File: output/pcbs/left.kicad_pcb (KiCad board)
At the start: 2 copper layers, 123.1 x 93.2 mm, 27 parts

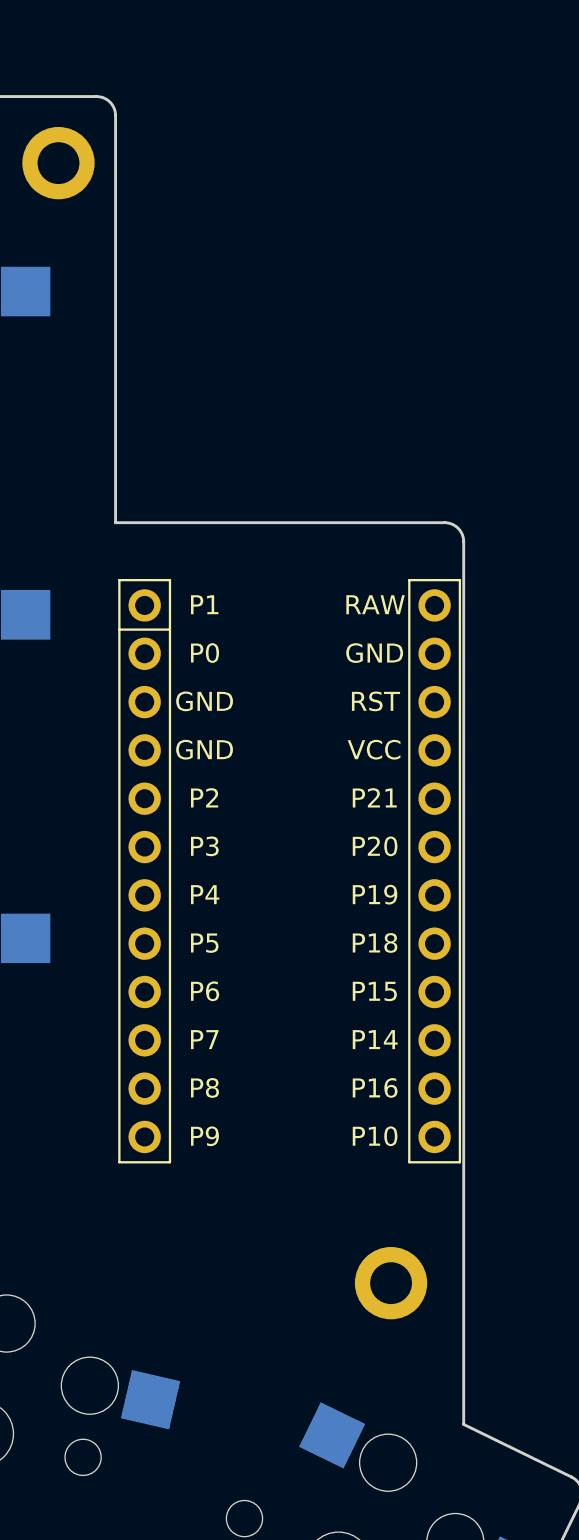
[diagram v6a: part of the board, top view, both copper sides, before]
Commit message: shift the MCU way up
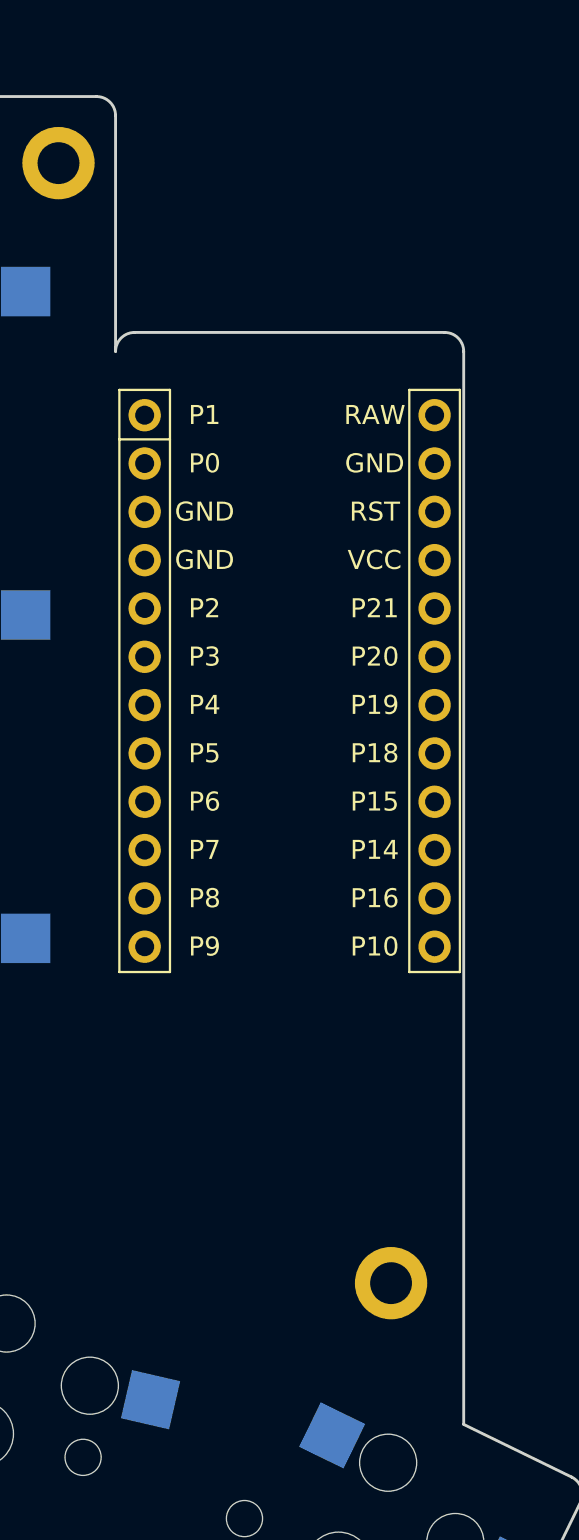
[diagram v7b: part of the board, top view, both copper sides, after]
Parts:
- moved MCU1 10.0 mm to (93.3, -31.4)
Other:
- outline, holes or cut-outs redrawn
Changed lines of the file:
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@@
   (footprint "ceoloide:mcu_nice_nano"
     (layer "F.Cu")
-    (at 93.29836660000001 -21.3657089 0)
+    (at 93.29836660000001 -31.3657089 0)
     (property "Reference" "MCU1"
       (at 0 -15 0)
@@
 (gr_line (start 108.1213601 11.751844899999998) (end 102.44836660000001 8.984941108545392) (layer Edge.Cuts) (stroke (width 0.15) (type default)))
 (gr_line (start 24.54726792343898 -60.815708799999996) (end 25.148366699999997 -60.84721104908856) (layer Edge.Cuts) (stroke (width 0.15) (type default)))
-(gr_line (start 84.1483667 -38.4157089) (end 101.44836660000001 -38.4157089) (layer Edge.Cuts) (stroke (width 0.15) (type default)))
-(gr_line (start 102.44836660000001 8.984941108545392) (end 102.44836660000001 -37.4157089) (layer Edge.Cuts) (stroke (width 0.15) (type default)))
-(gr_arc (start 102.44836660000001 -37.4157089) (mid 102.15547340000002 -38.1228157) (end 101.44836660000001 -38.4157089) (layer Edge.Cuts) (stroke (width 0.15) (type default)))
+(gr_line (start 102.44836660000001 8.984941108545392) (end 102.44836660000001 -47.4157089) (layer Edge.Cuts) (stroke (width 0.15) (type default)))
+(gr_line (start 85.1483666 -48.4157089) (end 101.44836660000001 -48.4157089) (layer Edge.Cuts) (stroke (width 0.15) (type default)))
+(gr_arc (start 85.1483666 -48.4157089) (mid 84.4414179 -48.1229738) (end 84.1483667 -47.4161561) (layer Edge.Cuts) (stroke (width 0.15) (type default)))
+(gr_arc (start 102.44836660000001 -47.4157089) (mid 102.15547340000002 -48.1228157) (end 101.44836660000001 -48.4157089) (layer Edge.Cuts) (stroke (width 0.15) (type default)))
 (gr_line (start -7.851633400000004 16.6842912) (end -8.3250278 16.460374) (layer Edge.Cuts) (stroke (width 0.15) (type default)))
 (gr_line (start -9.851633300000003 -42.7041617200161) (end -9.851633300000003 -59.815708799999996) (layer Edge.Cuts) (stroke (width 0.15) (type default)))
 (gr_line (start -8.851633300000003 -60.815708799999996) (end 24.54726792343898 -60.815708799999996) (layer Edge.Cuts) (stroke (width 0.15) (type default)))
 (gr_line (start 45.148366599999996 -60.815708799999996) (end 83.1483667 -60.815708799999996) (layer Edge.Cuts) (stroke (width 0.15) (type default)))
-(gr_line (start 84.1483667 -59.815708799999996) (end 84.1483667 -38.4157089) (layer Edge.Cuts) (stroke (width 0.15) (type default)))
+(gr_line (start 84.1483667 -59.815708799999996) (end 84.1483667 -47.4161561) (layer Edge.Cuts) (stroke (width 0.15) (type default)))
 (gr_arc (start -8.851633300000003 -60.815708799999996) (mid -9.558740100000003 -60.522815599999994) (end -9.851633300000003 -59.815708799999996) (layer Edge.Cuts) (stroke (width 0.15) (type default)))
 (gr_arc (start 84.1483667 -59.815708799999996) (mid 83.8554735 -60.522815599999994) (end 83.1483667 -60.815708799999996) (layer Edge.Cuts) (stroke (width 0.15) (type default)))

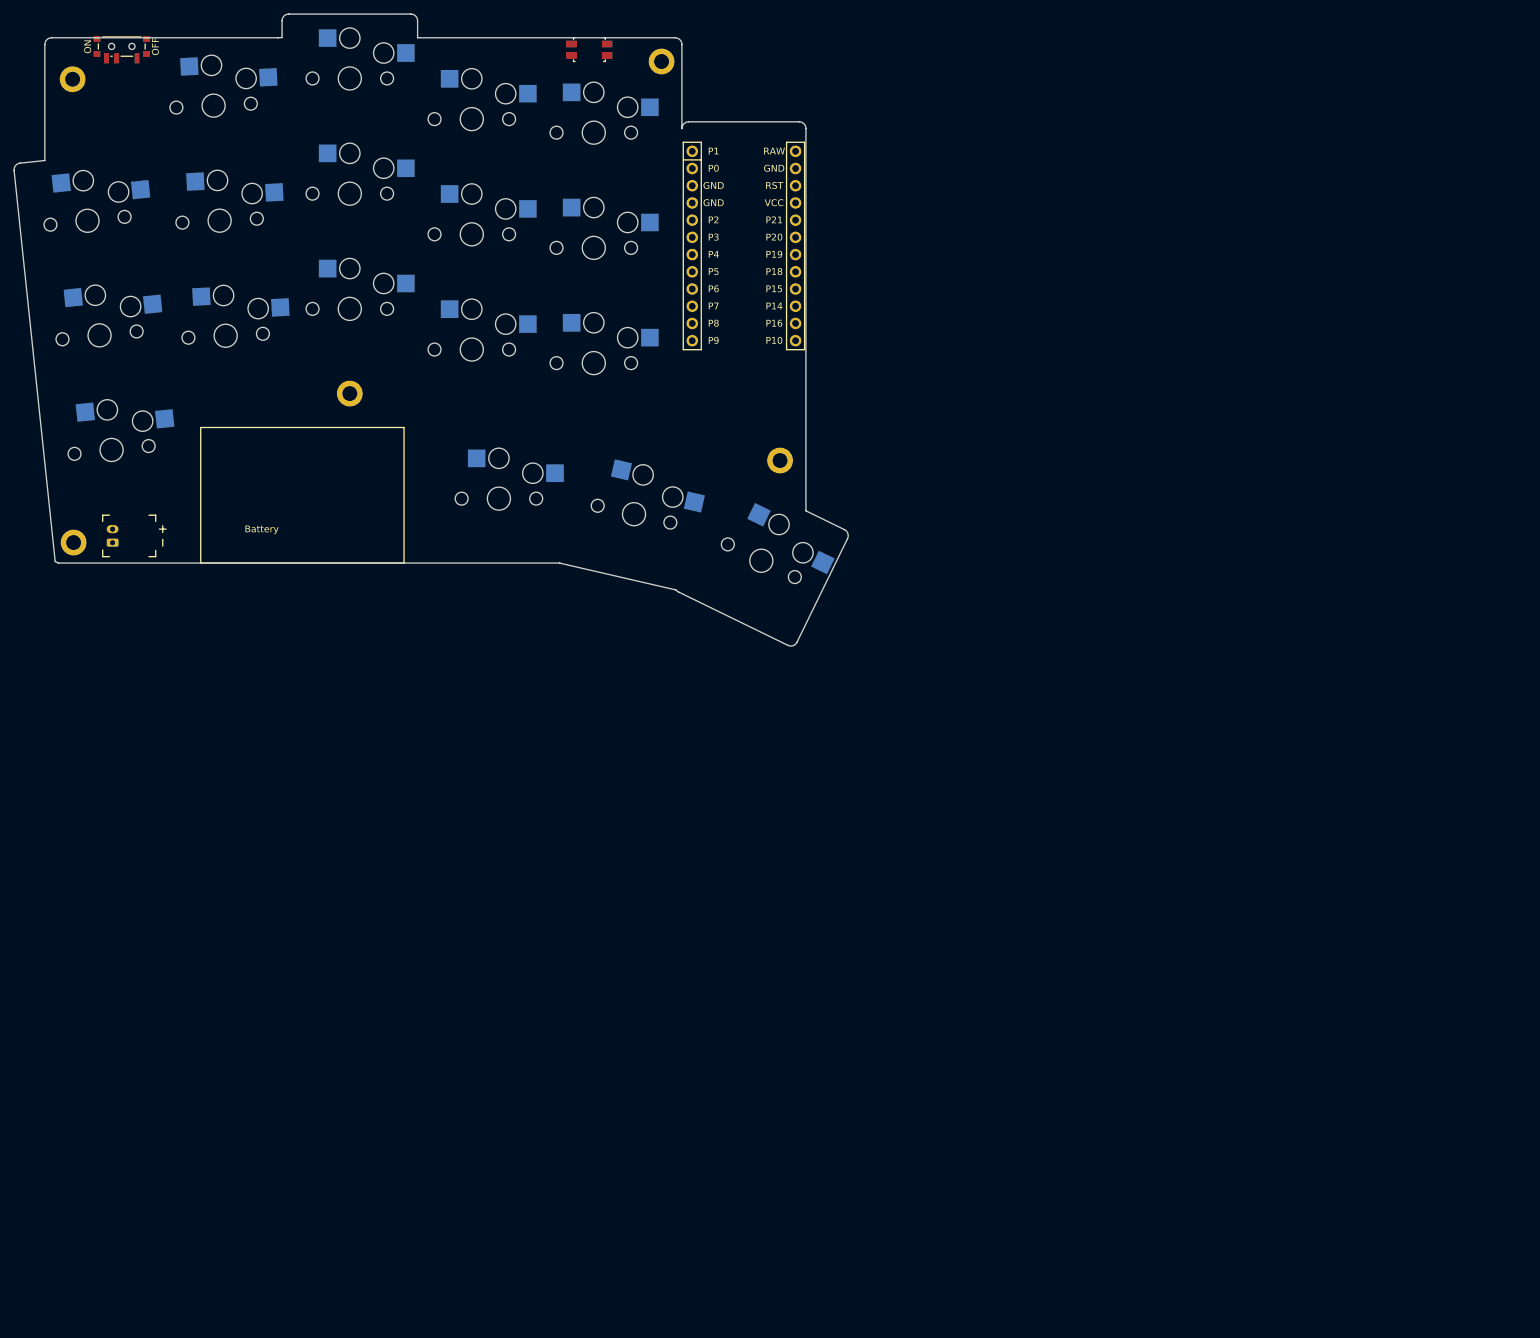
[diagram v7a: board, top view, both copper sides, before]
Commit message: Fix controller length
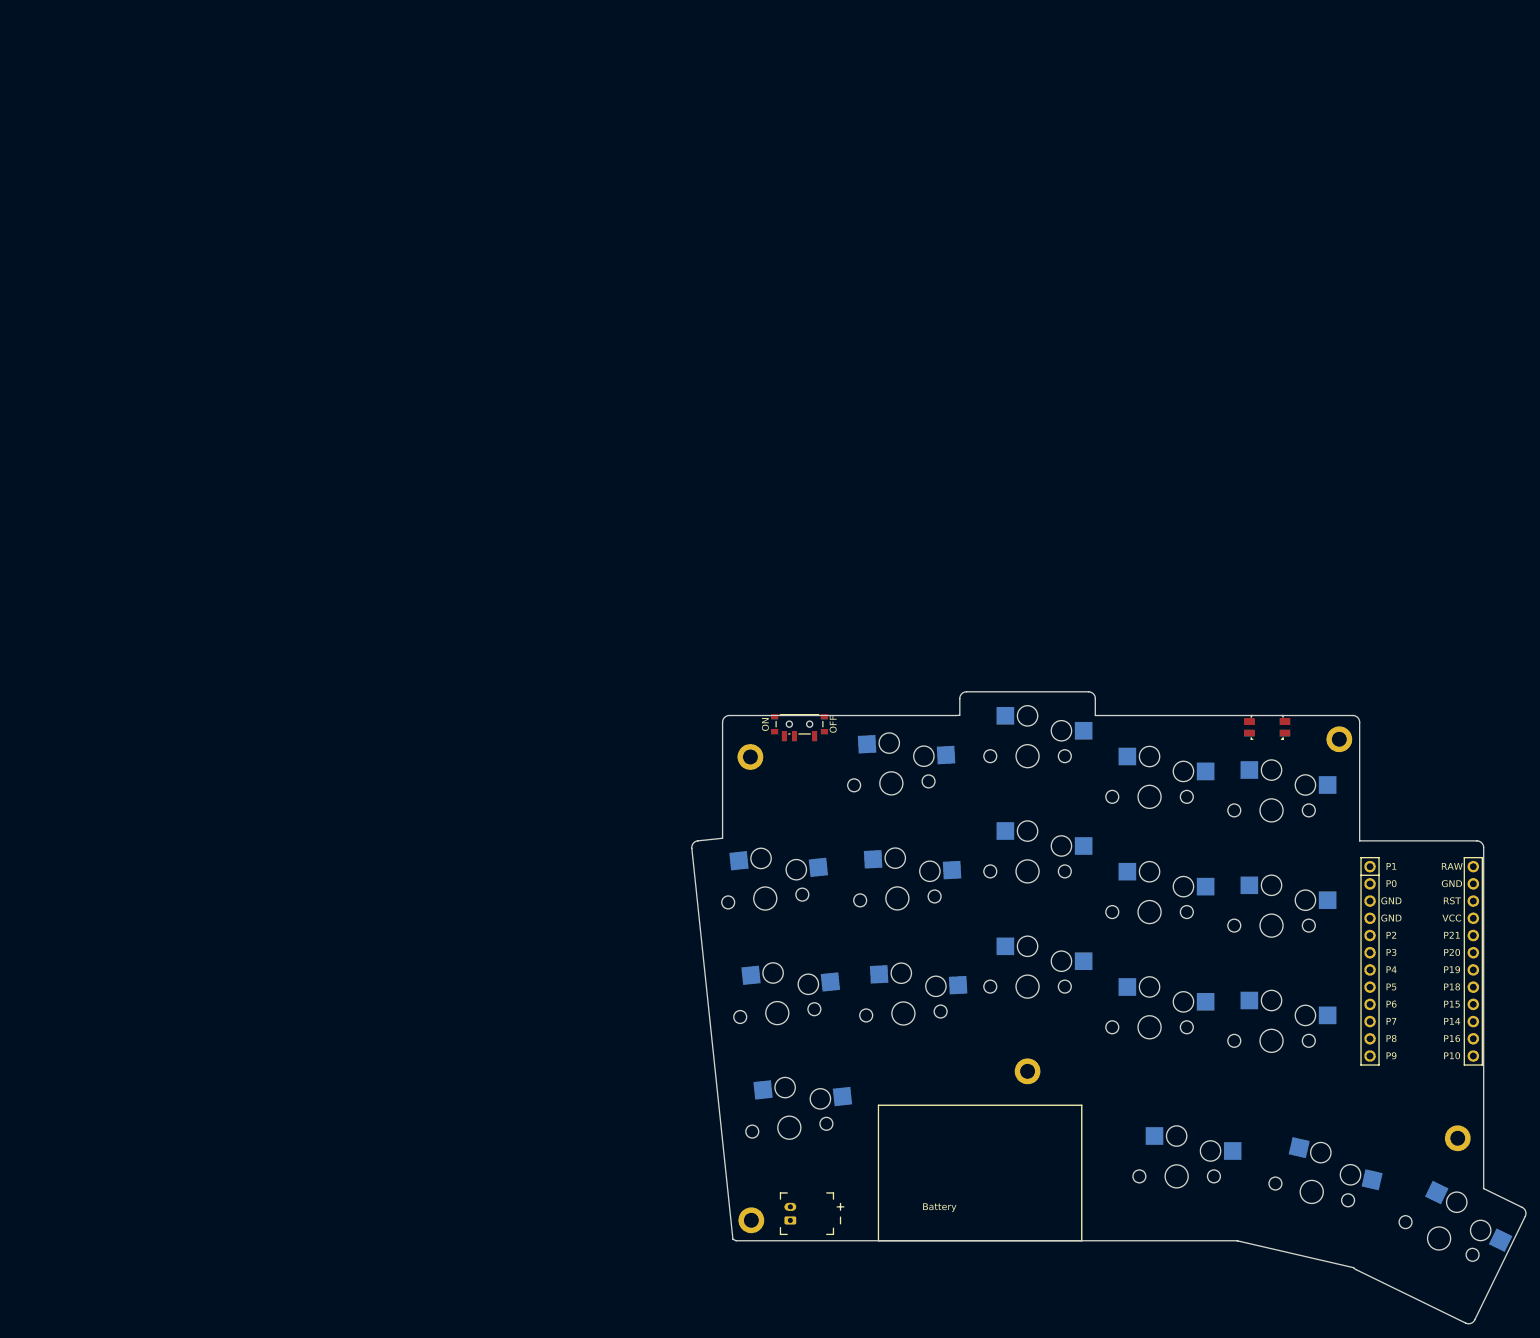
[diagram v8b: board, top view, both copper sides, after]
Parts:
- moved MCU1 145.4 mm to (193.3, 74.2)
- moved H2 141.4 mm to (181.1, 42.7)
- moved H3 141.4 mm to (94.4, 113.7)
- moved S1 141.4 mm to (100.0, 100.0)
- moved S13 141.4 mm to (171.1, 87.2)
- moved S14 141.4 mm to (171.1, 70.2)
- moved S15 141.4 mm to (171.1, 53.2)
- moved S18 141.4 mm to (195.9, 116.3)
- moved S2 141.4 mm to (98.2, 83.1)
- moved S4 141.4 mm to (116.8, 83.1)
- moved S5 141.4 mm to (115.9, 66.2)
- moved S6 141.4 mm to (115.1, 49.2)
- moved H1 141.4 mm to (94.3, 45.3)
- moved H4 141.4 mm to (135.1, 91.7)
- moved H5 141.4 mm to (198.6, 101.6)
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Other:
- outline, holes or cut-outs redrawn
